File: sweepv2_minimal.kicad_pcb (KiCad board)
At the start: 2 copper layers, 217.3 x 86.9 mm, 44 parts, among them J1 AudioJack4dpb, J2 AudioJack4dpb, SW10 SW_Push, SW11 SW_Push, SW11_r1 SW_Push, SW12 SW_Push, SW12_r1 SW_Push, SW13_r1 SW_Push, SW14 SW_Push, SW15 SW_Push, SW15_r1 SW_Push, SW16 SW_Push, SW16_r1 SW_Push, SW17 SW_Push, SW17_r1 SW_Push, SW18 SW_Push, SW18_r1 SW_Push, SW2 SW_Push, SW20 SW_Push, SW20_r1 SW_Push, SW21 SW_Push, SW21_r1 SW_Push, SW2_r1 SW_Push, SW3 SW_Push, SW3_r1 SW_Push, SW4 SW_Push, SW4_r1 SW_Push, SW5 SW_Push, SW5_r1 SW_Push, SW6 SW_Push, SW6_r1 SW_Push, SW7_r1 SW_Push, SW8 SW_Push, SW8_r1 SW_Push, SW9 SW_Push, SW9_r1 SW_Push, U1 ProMicro-kbd, U2 ProMicro-kbd

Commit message: Use minimalist file names
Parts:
- moved REF** 2.59 mm to (58.0, 75.3)
- moved REF** 1.94 mm to (186.4, 75.0)

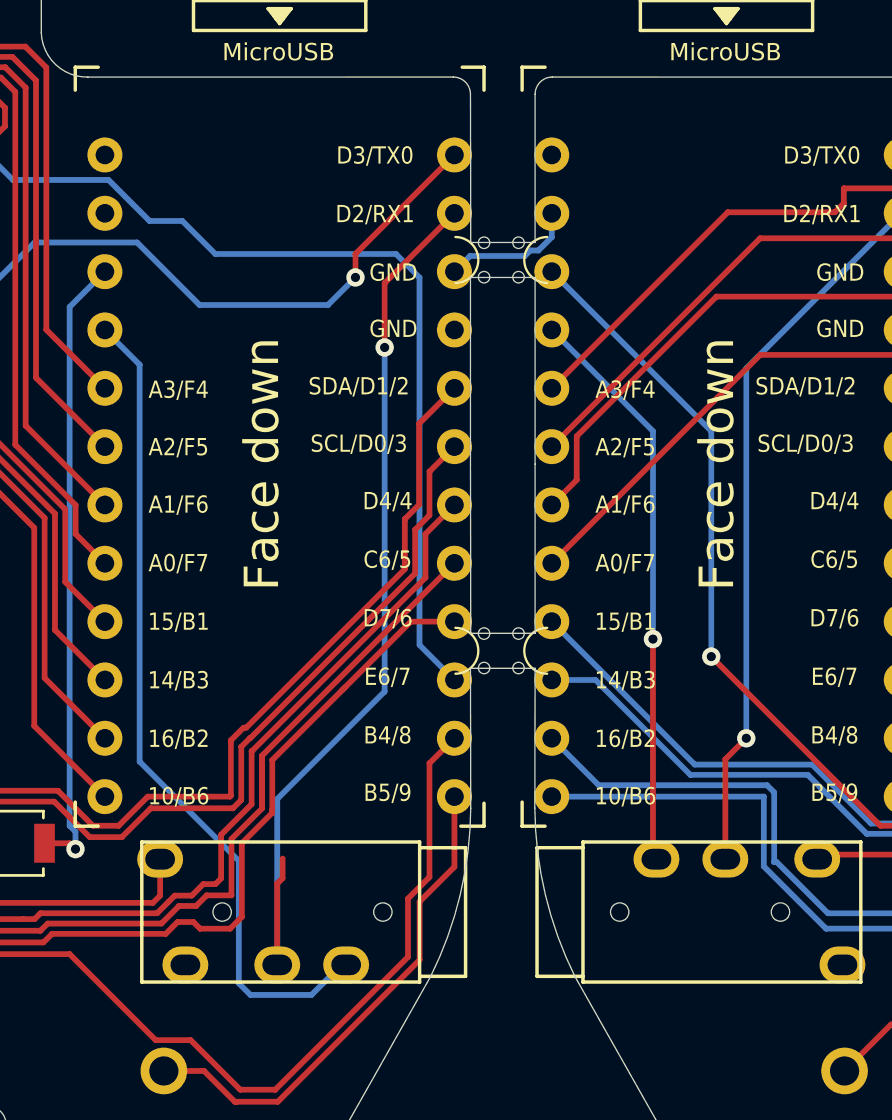
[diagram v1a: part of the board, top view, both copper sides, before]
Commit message: Remove incorrect Sweepv2 silk bottom, add custom architeuthis.dux
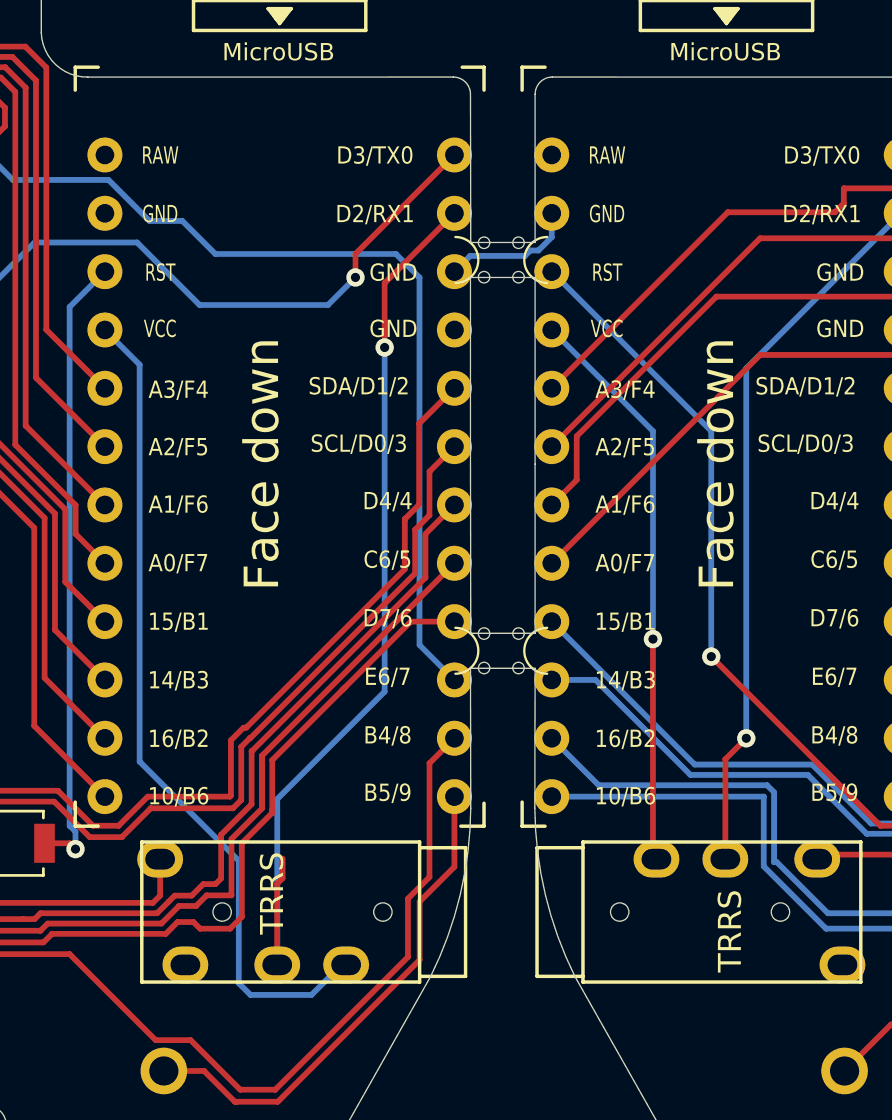
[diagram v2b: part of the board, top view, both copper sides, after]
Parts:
- added ?: , , F.Cu at (129.9, 45.2)
- added ?: , , F.Cu at (130.8, 51.2)
- added ?: , , F.Cu at (112.2, 50.8)
- added ?: , , F.Cu at (112.0, 33.7)
- added ?: , , F.Cu at (111.2, 51.6)
- added ?: , , F.Cu at (130.2, 45.9)
- added ?: , , F.Cu at (130.7, 48.6)
- added ?: , , F.Cu at (131.0, 49.4)
- added ?: , , F.Cu at (111.5, 47.0)
- added ?: , , F.Cu at (111.0, 47.4)
- added ?: , , F.Cu at (111.3, 49.6)
- added ?: , , F.Cu at (110.8, 49.5)
- added ?: , , F.Cu at (131.2, 50.8)

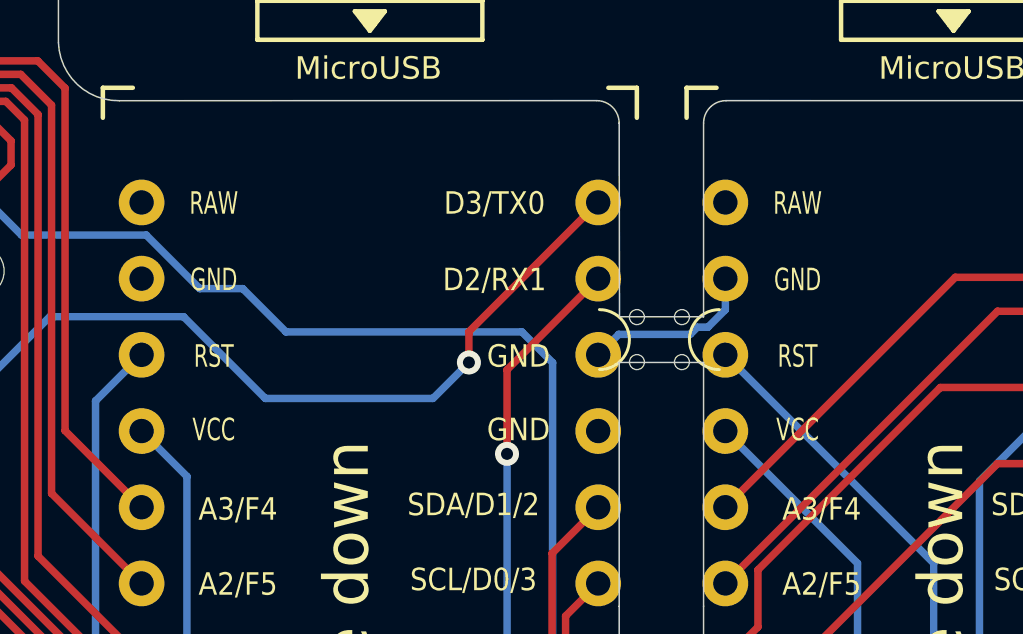
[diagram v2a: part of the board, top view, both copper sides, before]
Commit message: Replace Architeuthis.dux with no puck version
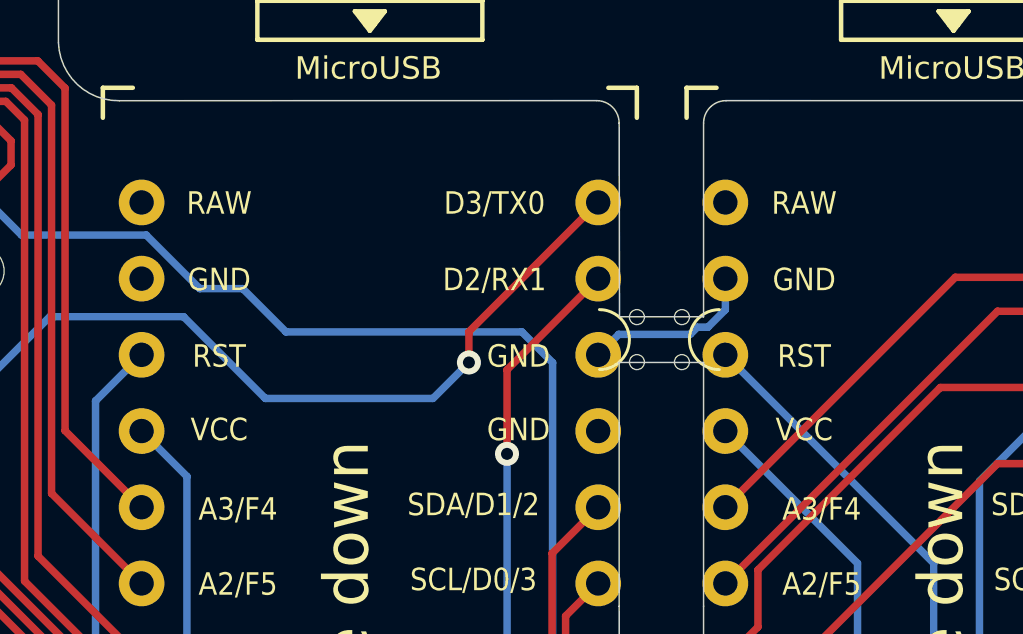
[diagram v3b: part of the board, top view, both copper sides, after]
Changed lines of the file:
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@@
       (effects (font (size 1.27 1.27) (thickness 0.15)))
     )
-    (fp_text user RAW (at -3.12 -0.448) (layer F.SilkS)
-      (effects (font (size 0.75 0.5) (thickness 0.125)))
+    (fp_text user RAW (at -2.9 -0.448) (layer F.SilkS)
+      (effects (font (size 0.75 0.67) (thickness 0.125)))
     )
   )
@@
       (effects (font (size 1.27 1.27) (thickness 0.15)))
     )
-    (fp_text user GND (at -3.47 1.402) (layer F.SilkS)
-      (effects (font (size 0.75 0.5) (thickness 0.125)))
+    (fp_text user GND (at -3.25 1.402) (layer F.SilkS)
+      (effects (font (size 0.75 0.67) (thickness 0.125)))
     )
   )
@@
       (effects (font (size 1.27 1.27) (thickness 0.15)))
     )
-    (fp_text user RST (at -3.91 1.182) (layer F.SilkS)
-      (effects (font (size 0.75 0.5) (thickness 0.125)))
+    (fp_text user RST (at -3.69 1.182) (layer F.SilkS)
+      (effects (font (size 0.75 0.67) (thickness 0.125)))
     )
   )
@@
       (effects (font (size 1.27 1.27) (thickness 0.15)))
     )
-    (fp_text user VCC (at -4.18 2.922) (layer F.SilkS)
-      (effects (font (size 0.75 0.5) (thickness 0.125)))
+    (fp_text user VCC (at -3.96 2.922) (layer F.SilkS)
+      (effects (font (size 0.75 0.67) (thickness 0.125)))
     )
   )
@@
       (effects (font (size 1.27 1.27) (thickness 0.15)))
     )
-    (fp_text user RAW (at -4.21 -2.268) (layer F.SilkS)
-      (effects (font (size 0.75 0.5) (thickness 0.125)))
+    (fp_text user RAW (at -4.03 -2.268) (layer F.SilkS)
+      (effects (font (size 0.75 0.67) (thickness 0.125)))
     )
   )
@@
       (effects (font (size 1.27 1.27) (thickness 0.15)))
     )
-    (fp_text user GND (at -3.73 -0.138) (layer F.SilkS)
-      (effects (font (size 0.75 0.5) (thickness 0.125)))
+    (fp_text user GND (at -3.55 -0.138) (layer F.SilkS)
+      (effects (font (size 0.75 0.67) (thickness 0.125)))
     )
   )
@@
       (effects (font (size 1.27 1.27) (thickness 0.15)))
     )
-    (fp_text user RST (at -4.02 0.222) (layer F.SilkS)
-      (effects (font (size 0.75 0.5) (thickness 0.125)))
+    (fp_text user RST (at -3.84 0.222) (layer F.SilkS)
+      (effects (font (size 0.75 0.67) (thickness 0.125)))
     )
   )
@@
       (effects (font (size 1.27 1.27) (thickness 0.15)))
     )
-    (fp_text user VCC (at -3.48 2.772) (layer F.SilkS)
-      (effects (font (size 0.75 0.5) (thickness 0.125)))
+    (fp_text user VCC (at -3.3 2.772) (layer F.SilkS)
+      (effects (font (size 0.75 0.67) (thickness 0.125)))
     )
   )
